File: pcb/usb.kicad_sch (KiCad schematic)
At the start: 42 parts, among them J6 USB4105-GF-A, J7 S2B-PH-SM4-TB, Q1 DMP3099L-7, Q2 DMG3418L, Q3 DMG3418L, SW1 400MSP1R6BLKM6QE, U151 AP2112K-3.3, U152 BQ29700DSER, U153 MCP73831T-2ACI/OT, U154 APX803L05-35SA-7

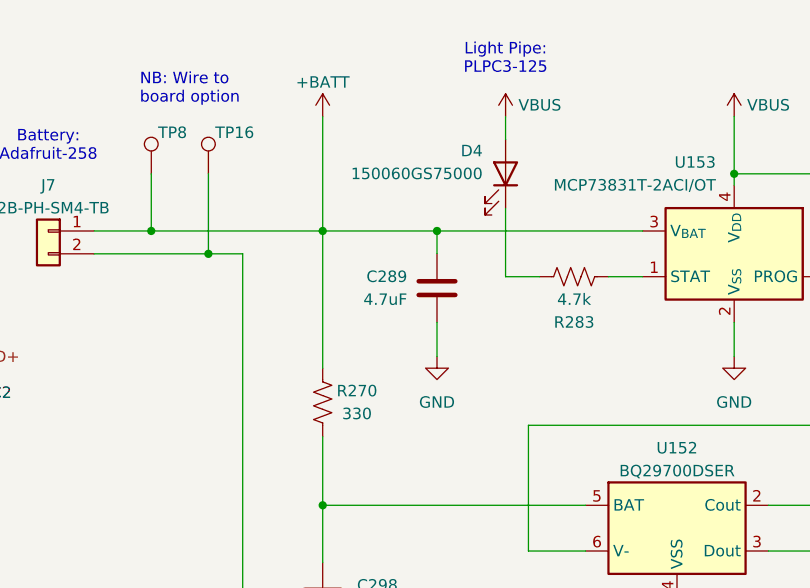
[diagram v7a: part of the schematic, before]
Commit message: Added OEPS PN.
Co-Authored-By: David Palma <78764277+davidpalma666@users.noreply.github.com>
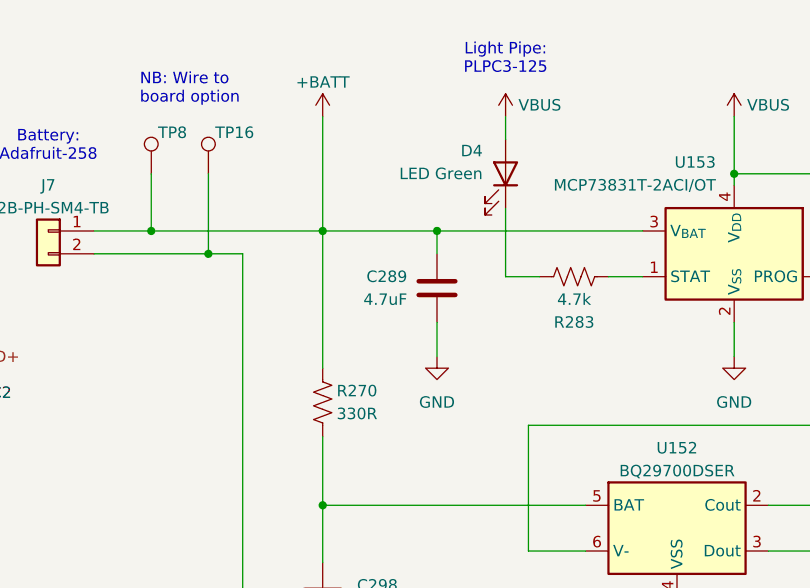
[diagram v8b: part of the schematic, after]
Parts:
- C289: MPN (none) -> CL31B475KOHNNNE; OEPSPN (none) -> OEPS010081
- C295, C297: MPN (none) -> CL10A105KA8NNNC; OEPSPN (none) -> OEPS010022
- C298, C307, C310: MPN (none) -> C1005X7R1E104K050BB; OEPSPN (none) -> OEPS010050
- C299: MPN (none) -> CL31B106KBHNNNE; OEPSPN (none) -> OEPS010032
- D3: MPN (none) -> CDBW140-G; OEPSPN (none) -> OEPS030034
- D4: value 150060GS75000 -> LED Green; MPN (none) -> 150060GS75000; OEPSPN (none) -> OEPS030033
- D9: MPN (none) -> TPD4E05U06DQAR; OEPSPN (none) -> OEPS030037
- J6: MPN (none) -> USB4105-GF-A; OEPSPN (none) -> OEPS070105
- J7: MPN (none) -> S2B-PH-SM4-TB; OEPSPN (none) -> OEPS070106
- Q1: MPN (none) -> DMP3099L-7; OEPSPN (none) -> OEPS060020
- Q2, Q3: MPN (none) -> DMG3418L-7; OEPSPN (none) -> OEPS060019
- R263: MPN (none) -> ERJ-2RKF4702X; OEPSPN (none) -> OEPS020017
- R264, R265: MPN (none) -> CRCW040210K0FKED; OEPSPN (none) -> OEPS020030
- R266, R267: MPN (none) -> ERJ-2RKF5101X; OEPSPN (none) -> OEPS020173
- R270: value 330 -> 330R; MPN (none) -> CRCW0603330RFKEAC; OEPSPN (none) -> OEPS020139
- R271, R283: MPN (none) -> ERJ-2RKF4701X; OEPSPN (none) -> OEPS020010
- R272: MPN (none) -> ERJ-2RKF2201X; OEPSPN (none) -> OEPS020174
- SW1: MPN (none) -> 400MSP1R6BLKM6QE; OEPSPN (none) -> OEPS070112
- TP1, TP10, TP14, TP15, TP16, TP2, TP3, TP4, TP5, TP6, TP7, TP8, TP9: now left out of the parts list
- U151: MPN (none) -> AP2112K-3.3TRG1; OEPSPN (none) -> OEPS080155
- U152: MPN (none) -> BQ29700DSER; OEPSPN (none) -> OEPS080156
- U153: MPN (none) -> MCP73831T-2ACI/OT; OEPSPN (none) -> OEPS080157
- U154: MPN (none) -> APX803L05-35SA-7; OEPSPN (none) -> OEPS080168
